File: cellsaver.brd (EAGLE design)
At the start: 50 x 19 mm, 31 parts, among them Q11 2PMOS30V_4.5A, Q21 2PMOS30V_4.5A, Q22 2PMOS30V_4.5A, Q31 2PMOS30V_4.5A, Q32 2PMOS30V_4.5A, Q41 2PMOS30V_4.5A, Q42 2PMOS30V_4.5A, Q51 2PMOS30V_4.5A, Q52 2PMOS30V_4.5A, Q61 2PMOS30V_4.5A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

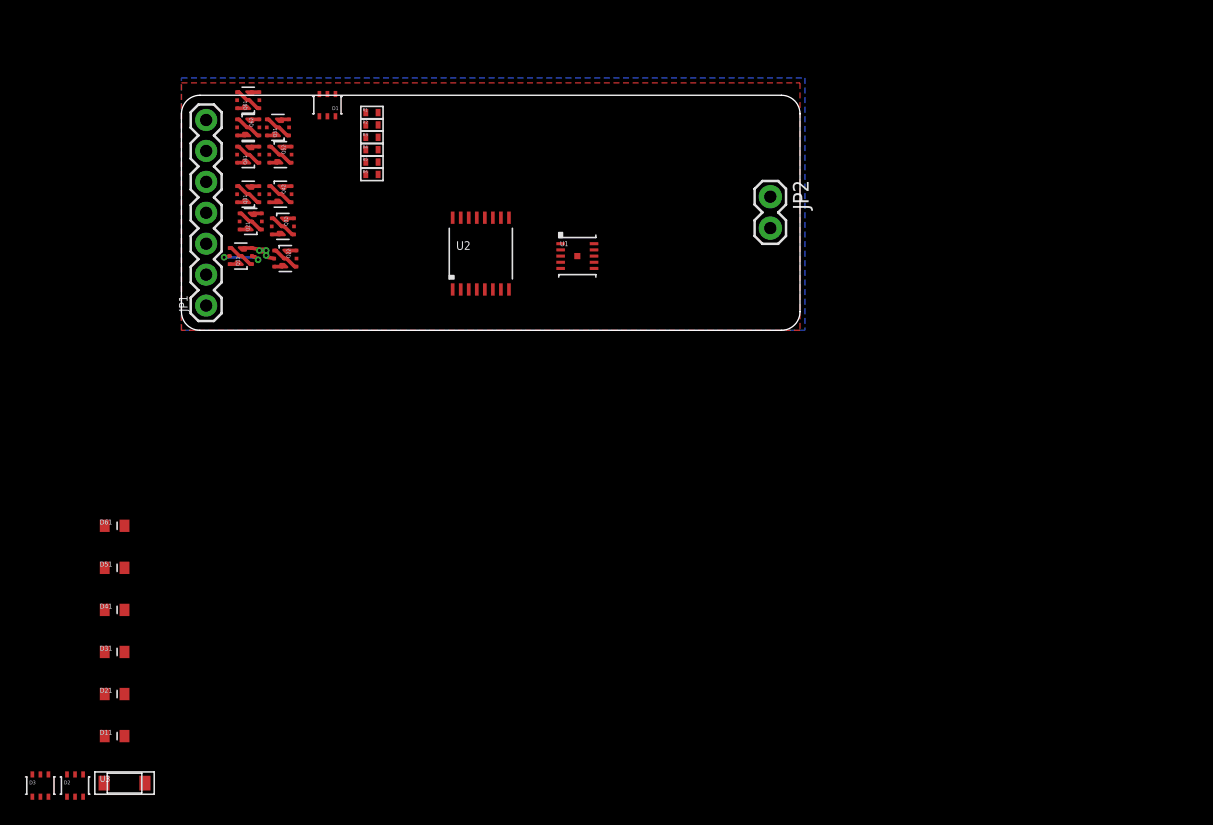
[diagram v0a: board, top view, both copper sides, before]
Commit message: FET change, layout
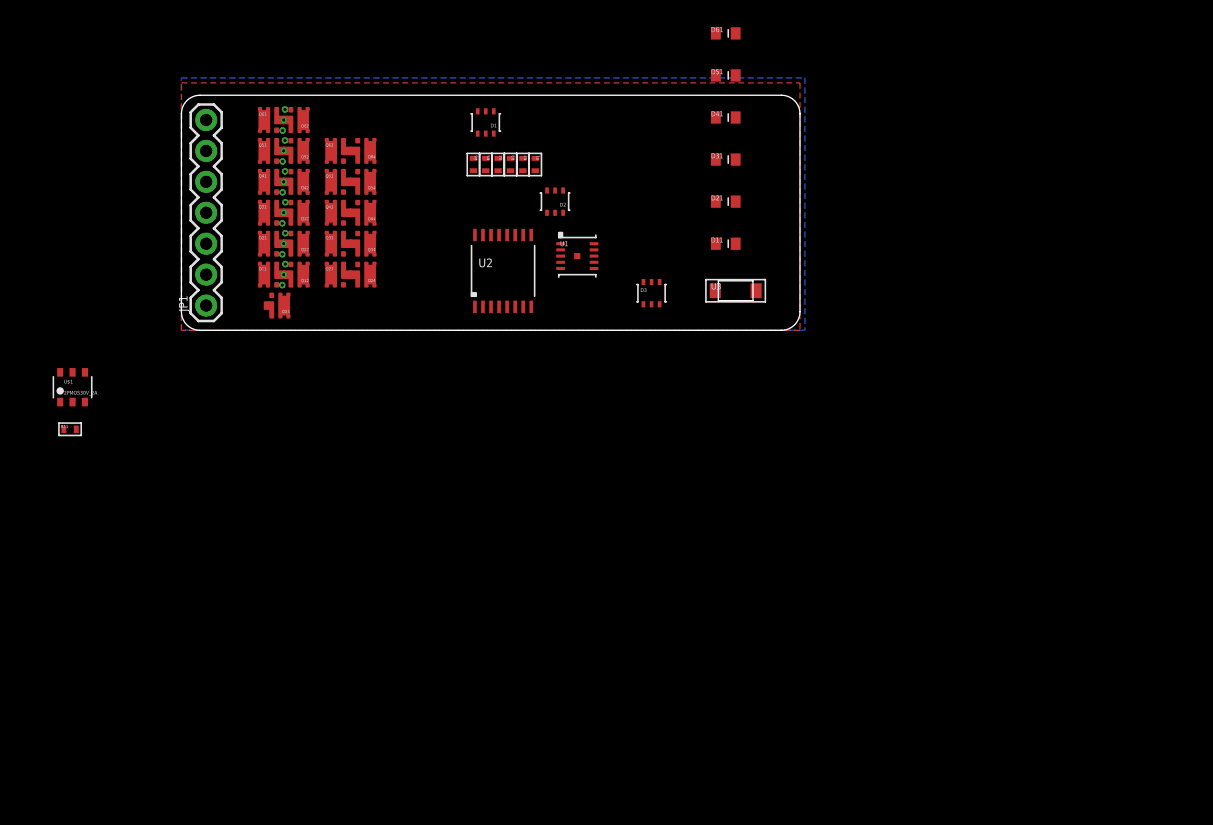
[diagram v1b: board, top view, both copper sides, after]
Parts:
- removed JP2: M02PTH, SparkFun-Connectors:1X02
- added Q12, Q23, Q24, Q33, Q34, Q43, Q44, Q53, Q54, Q63, Q64: PMOS30V_11A, dubec:6-POWERWDFN
- added Q13: NMOS40V_10A, dubec:6-POWERWDFN
- added R11: RES100K_16, dubec:0402
- added U$1: 2PMOS30V_2A, dubec:6-TSOP
- Q11, Q21, Q22, Q31, Q32, Q41, Q42, Q51, Q52, Q61, Q62: value 2PMOS30V_4.5A -> PMOS30V_11A; device dubec:SC70-6L-CS -> dubec:6-POWERWDFN
- moved U3 63.4 mm to (44.8, 3.20)
- moved D11 63.4 mm to (44.0, 7.00)
- moved D21 63.4 mm to (44.0, 10.4)
- moved D3 63.4 mm to (38.0, 3.00)
- moved D31 63.4 mm to (44.0, 13.8)
- moved D41 63.4 mm to (44.0, 17.2)
- moved D51 63.4 mm to (44.0, 20.6)
- moved D61 63.4 mm to (44.0, 24.0)
- moved D2 61.1 mm to (30.2, 10.4), turned to 180 degrees
- moved R1 13.9 mm to (28.6, 13.4), turned to 270 degrees
- moved D1 12.9 mm to (24.6, 16.8)
- moved R2 12.6 mm to (27.6, 13.4), turned to 270 degrees
- moved R3 11.4 mm to (26.6, 13.4), turned to 270 degrees
- moved R4 10.3 mm to (25.6, 13.4), turned to 270 degrees
- moved R5 9.20 mm to (24.6, 13.4), turned to 270 degrees
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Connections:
- removed net S+1: Q11.1, Q11.4
- removed net S+2: Q21.1, Q21.4
- removed net S+3: Q31.1, Q31.4
- removed net S+4: Q41.1, Q41.4
- removed net S+5: Q51.1, Q51.4
- removed net S+6: Q61.1, Q61.4
- removed net S-2: Q22.1, Q22.4
- removed net S-3: Q32.1, Q32.4
- removed net S-4: Q42.1, Q42.4
- removed net S-5: Q52.1, Q52.4
- removed net S-6: Q62.1, Q62.4
- removed net T+: Q11.3, Q11.D2, Q21.3, Q21.D2, Q31.3, Q31.D2, Q41.3, Q41.D2, Q51.3, Q51.D2, Q61.3, Q61.D2
- removed net T-: Q22.6, Q22.D1, Q32.6, Q32.D1, Q42.6, Q42.D1, Q52.6, Q52.D1, Q62.6, Q62.D1
- new net G01: Q13.G, R11.2, U$1.6
- new net G11: Q11.G, Q12.G, U$1.1
- new net G21: Q21.G, Q22.G, Q23.G, Q24.G
- new net G31: Q31.G, Q32.G, Q33.G, Q34.G
- new net G41: Q41.G, Q42.G, Q43.G, Q44.G
- new net G51: Q51.G, Q52.G, Q53.G, Q54.G
- new net G61: Q61.G, Q62.G, Q63.G, Q64.G
- new net S+11: Q11.S, Q12.S
- new net S+21: Q21.S, Q22.S
- new net S+31: Q31.S, Q32.S
- new net S+41: Q41.S, Q42.S
- new net S+51: Q51.S, Q52.S
- new net S+61: Q61.S, Q62.S
- new net S-: Q13.D, Q24.D, Q34.D, Q44.D, Q54.D, Q64.D
- new net S-21: Q23.S, Q24.S
- new net S-31: Q33.S, Q34.S
- new net S-41: Q43.S, Q44.S
- new net S-51: Q53.S, Q54.S
- new net S-61: Q63.S, Q64.S
- new net VCC: U1.10
- net C0: now also Q13.S, R11.1
- net C1: now also Q11.D, Q23.D, U$1.5; no longer Q11.6, Q11.D1, Q22.3, Q22.D2
- net C2: now also Q21.D, Q33.D; no longer Q21.6, Q21.D1, Q32.3, Q32.D2
- net C3: now also Q31.D, Q43.D; no longer Q31.6, Q31.D1, Q42.3, Q42.D2
- net C4: now also Q41.D, Q53.D; no longer Q41.6, Q41.D1, Q52.3, Q52.D2
- net C5: now also Q51.D, Q63.D; no longer Q51.6, Q51.D1, Q62.3, Q62.D2
- net C6: now also Q61.D; no longer Q61.6, Q61.D1
- net G1: no longer Q11.2, Q11.5
- net G2: no longer Q21.2, Q21.5, Q22.2, Q22.5
- net G3: no longer Q31.2, Q31.5, Q32.2, Q32.5
- net G4: no longer Q41.2, Q41.5, Q42.2, Q42.5
- net G5: no longer Q51.2, Q51.5, Q52.2, Q52.5
- net G6: no longer Q61.2, Q61.5, Q62.2, Q62.5
- net GND: no longer JP2.2
- net N$12: now also D2.2
- net N$14: now also D3.1
- net N$15: now also D3.2
- net N$16: now also D3.3
- net S+: now also Q12.D, Q22.D, Q32.D, Q42.D, Q52.D, Q62.D; no longer JP2.1, U1.10
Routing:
- net G1: track 3.89 -> 0.00 mm
- net T+: track 1.20 -> 0.00 mm, vias 2 -> 0
- net G2: track 0.72 -> 0.00 mm, vias 1 -> 2

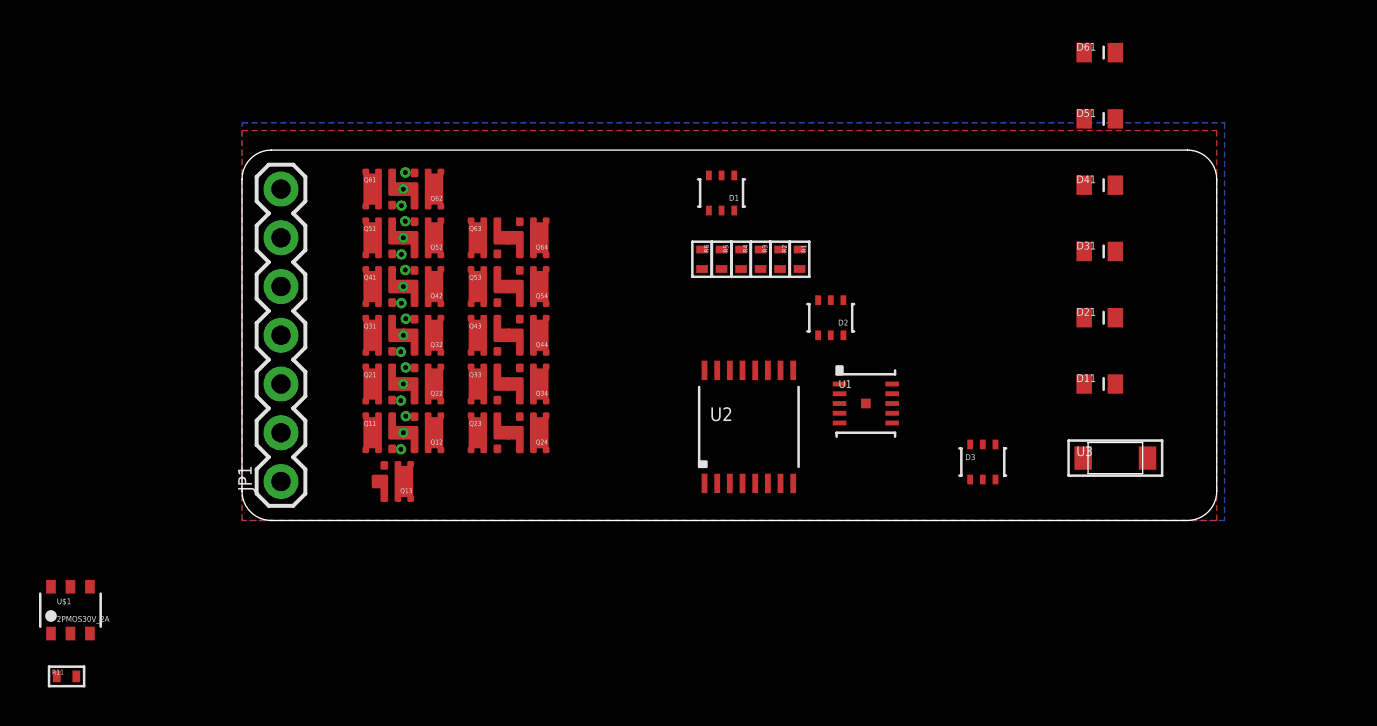
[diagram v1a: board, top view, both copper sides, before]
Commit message: Second pair of rails, for direct contact
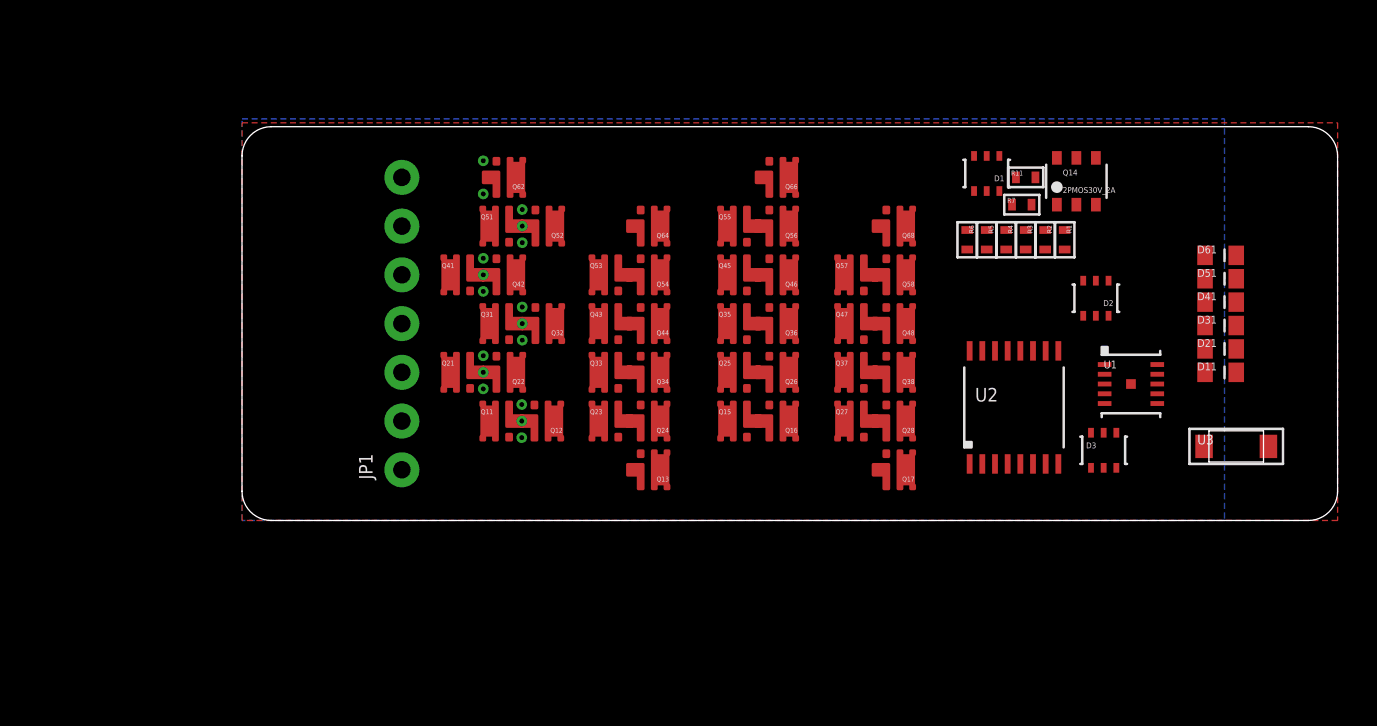
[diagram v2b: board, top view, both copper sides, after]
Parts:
- removed Q61, Q63: PMOS30V_11A, dubec:6-POWERWDFN
- removed U$1: 2PMOS30V_2A, dubec:6-TSOP
- added Q14: 2PMOS30V_2A, dubec:6-TSOP
- added Q15, Q16, Q25, Q26, Q27, Q28, Q35, Q36, Q37, Q38, Q45, Q46, Q47, Q48, Q55, Q56, Q57, Q58, Q66, Q68: PMOS30V_11A, dubec:6-POWERWDFN
- added Q17: NMOS40V_10A, dubec:6-POWERWDFN
- added R7: RES100K_16, dubec:0402
- JP1: value M07 -> M07XHRA; device dubec:1X07 -> dubec:XH07-RA
- moved R11 55.5 mm to (40.2, 17.6)
- moved D1 13.6 mm to (38.2, 17.8)
- moved R1 13.6 mm to (42.2, 14.4)
- moved R2 13.6 mm to (41.2, 14.4)
- moved R3 13.6 mm to (40.2, 14.4)
- moved R4 13.6 mm to (39.2, 14.4)
- moved R5 13.6 mm to (38.2, 14.4)
- moved R6 13.6 mm to (37.2, 14.4)
- moved U1 13.6 mm to (45.6, 7.00)
- moved U2 13.6 mm to (39.6, 5.80)
- moved D2 13.6 mm to (43.8, 11.4)
- moved Q13 13.2 mm to (21.1, 2.60)
- moved D61 12.1 mm to (50.2, 13.6)
- moved D51 10.3 mm to (50.2, 12.4)
- moved D41 8.63 mm to (50.2, 11.2)
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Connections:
- removed net G1: D3.4, R6.2, U2.5
- removed net G2: D3.5, R5.2, U2.6
- removed net G3: D3.6, R4.2, U2.7
- removed net G4: D2.4, R3.2, U2.12
- removed net G5: D2.5, R2.2, U2.11
- removed net G6: D2.6, R1.2, U2.10
- removed net S+61: Q61.S, Q62.S
- removed net S-61: Q63.S, Q64.S
- new net G02: Q14.4, Q17.G, R7.2
- new net G12: Q14.3, Q15.G, Q16.G
- new net G22: Q25.G, Q26.G, Q27.G, Q28.G
- new net G32: Q35.G, Q36.G, Q37.G, Q38.G
- new net G42: Q45.G, Q46.G, Q47.G, Q48.G
- new net G52: Q55.G, Q56.G, Q57.G, Q58.G
- new net G62: Q66.G, Q68.G
- new net S+12: Q15.S, Q16.S
- new net S+22: Q25.S, Q26.S
- new net S+32: Q35.S, Q36.S
- new net S+42: Q45.S, Q46.S
- new net S+52: Q55.S, Q56.S
- new net S-22: Q27.S, Q28.S
- new net S-32: Q37.S, Q38.S
- new net S-42: Q47.S, Q48.S
- new net S-52: Q57.S, Q58.S
- new net T+: Q16.D, Q26.D, Q36.D, Q46.D, Q56.D, Q66.D
- new net T-: Q17.D, Q28.D, Q38.D, Q48.D, Q58.D, Q68.D
- net C0: now also JP1.7, Q17.S, R7.1; no longer JP1.1
- net C1: now also JP1.6, Q14.2, Q14.5, Q15.D, Q27.D; no longer JP1.2, U$1.5
- net C2: now also JP1.5, Q25.D, Q37.D; no longer JP1.3
- net C3: now also Q35.D, Q47.D
- net C4: now also JP1.3, Q45.D, Q57.D; no longer JP1.5
- net C5: now also JP1.2, Q55.D, Q64.S, Q68.S; no longer JP1.6, Q63.D
- net C6: now also JP1.1, Q62.S, Q66.S; no longer JP1.7, Q61.D
- net G01: now also Q14.6; no longer U$1.6
- net G11: now also D3.4, Q14.1, R6.2, U2.5; no longer U$1.1
- net G21: now also D3.5, R5.2, U2.6
- net G31: now also D3.6, R4.2, U2.7
- net G41: now also D2.4, R3.2, U2.12
- net G51: now also D2.5, R2.2, U2.11
- net G61: now also D2.6, R1.2, U2.10; no longer Q61.G, Q63.G
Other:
- board size 50 x 19 mm -> 56.2 x 20.2 mm

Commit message: Bootstrap power, FET optimization
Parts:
- removed Q14: 2PMOS30V_2A, dubec:6-TSOP
- removed Q24: PMOS30V_11A, dubec:6-POWERWDFN
- removed R6: RES100K_16, dubec:0402
- added D4, DG1: 4DSCH30V_0A1, dubec:8-HMD
- added Q01: NMOS40V_10A, dubec:6-POWERWDFN
- added R12, RG51, RG61: RES100K_16, dubec:0402
- added U$1: TCAP330UF_6.3V, dubec:1210+
- D1: value 2X2D_SCHOTTKY100V_0.125A -> 4DSCH30V_0A1; device dubec:SOT-363 -> dubec:8-HMD
- Q13: value NMOS40V_10A -> 2PMOS30V_2A; device dubec:6-POWERWDFN -> dubec:6-TSOP
- R1, R2: value RES100K_16 -> RES4.22K_16
- moved R2 49.8 mm to (0.00, -13.6), turned to 0 degrees
- moved R1 49.5 mm to (0.00, -11.4), turned to 0 degrees
- moved D1 33.4 mm to (4.80, 18.6)
- moved Q13 26.2 mm to (42.8, 17.4), turned to 0 degrees
- moved R11 13.2 mm to (53.4, 17.0)
- moved Q11 2.04 mm to (11.0, 5.50)
- moved Q12 1.50 mm to (14.2, 5.50)
- moved Q23 0.60 mm to (18.1, 5.50), turned to 180 degrees
- moved JP1 0.45 mm to (8.00, 10.5)
- moved Q21 0.40 mm to (11.0, 8.00)
- moved Q22 0.40 mm to (13.8, 8.00)
- moved Q31 0.40 mm to (13.0, 10.5)
- moved Q32 0.40 mm to (15.8, 10.5)
- moved Q41 0.40 mm to (11.0, 13.0)
- moved Q42 0.40 mm to (13.8, 13.0)
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- renumbered Q17 to Q03, R3 to RG41, R4 to RG31, R5 to RG21
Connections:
- removed net C0: JP1.7, Q03.S, Q13.S, R11.1, R7.1, U2.14, U2.3, U2.4, U2.8, U2.9
- removed net CMAX: U2.13
- removed net G01: Q13.G, Q14.6, R11.2
- removed net G12: Q14.3, Q15.G, Q16.G
- removed net GND: U1.11, U1.5
- removed net S+11: Q11.S, Q12.S
- new net BATT+: D1.5, D1.6, D1.7, D1.8, D4.6, RG21.1, RG31.1, RG41.1, RG51.1, RG61.1, U2.13
- new net BATT-: JP1.7, Q01.S, Q03.S, R12.1, R7.1, U2.4
- new net G13: Q13.3, Q15.G, Q16.G
- new net N$17: Q12.G, Q13.6, R12.2
- new net N$18: DG1.1, DG1.2, Q11.G
- net C1: now also Q13.2, Q13.5; no longer Q14.2, Q14.5, Q23.D, U2.2
- net C2: now also D1.1, R11.1; no longer D1.5
- net C3: now also D1.2; no longer D1.4
- net C4: now also D1.3; no longer D1.2
- net C5: now also D1.4; no longer D1.1
- net C6: now also D4.3; no longer D1.3, D1.6, R1.1, R2.1, R6.1, RG21.1, RG31.1, RG41.1
- net G02: now also Q13.4; no longer Q14.4
- net G11: now also DG1.8, Q01.G, Q13.1, R11.2; no longer Q11.G, Q12.G, Q14.1, R6.2
- net G21: now also DG1.7; no longer Q24.G
- net G51: now also RG51.2; no longer R2.2
- net G61: now also RG61.2; no longer R1.2
- net S+: now also D4.1, D4.2, R1.2
- net S-: now also Q01.D, Q23.D, R1.1, U$1.C, U1.11, U1.5; no longer Q13.D, Q24.D
- net S-21: now also Q11.S, Q12.S; no longer Q24.S
- net T+: now also R2.2
- net T-: now also R2.1
- net VCC: now also D4.7, D4.8, U$1.A, U2.2
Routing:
- net S-21: track 0.00 -> 3.25 mm, vias 0 -> 4
- net N$18: track 0.00 -> 0.48 mm, vias 0 -> 1
- net N$17: track 0.00 -> 0.48 mm, vias 0 -> 1
- added copper zone on layer 1, net BATT-
- added copper zone on layer 16, net BATT-
- removed copper zone on layer 1, net GND
- removed copper zone on layer 16, net GND
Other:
- board size 56.2 x 20.2 mm -> 56.2 x 21 mm

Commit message: .
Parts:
- added U$2: TFORM_4_4311_4A4, dubec:EPQ13
- moved R2 33.3 mm to (29.4, 2.00), turned to 180 degrees
- moved DG1 27.0 mm to (74.4, 16.6)
- moved R11 27.0 mm to (80.4, 15.8)
- moved R12 27.0 mm to (80.4, 16.8)
- moved D11 27.0 mm to (77.2, 6.40)
- moved D2 27.0 mm to (70.8, 10.2)
- moved D21 27.0 mm to (77.2, 7.60)
- moved D3 27.0 mm to (71.2, 2.40)
- moved D31 27.0 mm to (77.2, 8.80)
- moved D4 27.0 mm to (59.6, 17.8)
- moved D41 27.0 mm to (77.2, 10.0)
- moved D51 27.0 mm to (77.2, 11.2)
- moved D61 27.0 mm to (77.2, 12.4)
- moved Q13 27.0 mm to (69.8, 16.2)
- moved R7 27.0 mm to (67.0, 15.0)
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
